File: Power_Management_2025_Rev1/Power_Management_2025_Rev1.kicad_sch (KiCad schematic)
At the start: 103 parts, among them J1 RJ45_LED_Shielded, Q1 BSS138, Q2 IPB180N10S4-02, Q3 IPB180N10S4-02, U1 Teensy4.1_DEV-16771, U10 LT1910, U11 LT1910, U12 PKE3316ZPI, U13 PKE3316ZPI, U2 OKI-78SR-3.3_1.5-W36-C, U3 ACS756xCB-050B-PFF, U4 ${SIM.PARAMS}, U5 ${SIM.PARAMS}, U6 ${SIM.PARAMS}, U7 ${SIM.PARAMS}, U8 ${SIM.PARAMS}, U9 ${SIM.PARAMS}

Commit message: Added set of andersons
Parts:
- added unit 4 of Conn21
- added Conn24: AndersonPP, symbol MRDT_Connectors:AndersonPP
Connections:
- net GND: now also Conn24.1 (GND)
- net PV: now also Conn21.4 (PV+)
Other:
- moved on the sheet: Conn19A, Conn19D, Conn1E, Conn20A, Conn20D, Conn21A, Conn22A, Conn4E

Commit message: Cleaned up schematic
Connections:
- net GND: now also U1.USB_GND1 (USB_GND), U1.USB_GND2 (USB_GND)
- no-connect marks 5 -> 47
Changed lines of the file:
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@@
 	)
 	(junction
+		(at 86.36 123.19)
+		(diameter 0)
+		(color 0 0 0 0)
+	)
+	(junction
 		(at 227.965 118.11)
 		(diameter 0)
@@
 	)
 	(no_connect
+		(at 38.1 82.55)
+	)
+	(no_connect
+		(at 196.85 248.92)
+	)
+	(no_connect
+		(at 78.74 80.01)
+	)
+	(no_connect
+		(at 78.74 77.47)
+	)
+	(no_connect
+		(at 78.74 54.61)
+	)
+	(no_connect
+		(at 275.59 238.76)
+	)
+	(no_connect
+		(at 38.1 87.63)
+	)
+	(no_connect
+		(at 38.1 39.37)
+	)
+	(no_connect
+		(at 38.1 67.31)
+	)
+	(no_connect
+		(at 38.1 62.23)
+	)
+	(no_connect
+		(at 78.74 74.93)
+	)
+	(no_connect
+		(at 78.74 113.03)
+	)
+	(no_connect
+		(at 38.1 90.17)
+	)
+	(no_connect
+		(at 78.74 100.33)
+	)
+	(no_connect
 		(at 62.23 139.7)
 	)
 	(no_connect
+		(at 38.1 85.09)
+	)
+	(no_connect
+		(at 78.74 67.31)
+	)
+	(no_connect
+		(at 38.1 59.69)
+	)
+	(no_connect
+		(at 38.1 69.85)
+	)
+	(no_connect
+		(at 38.1 46.99)
+	)
+	(no_connect
+		(at 78.74 34.29)
+	)
+	(no_connect
 		(at 62.23 142.24)
 	)
 	(no_connect
+		(at 78.74 115.57)
+	)
+	(no_connect
+		(at 78.74 102.87)
+	)
+	(no_connect
 		(at 41.91 154.94)
 	)
 	(no_connect
+		(at 78.74 97.79)
+	)
+	(no_connect
+		(at 38.1 64.77)
+	)
+	(no_connect
 		(at 365.76 166.37)
 	)
 	(no_connect
+		(at 38.1 49.53)
+	)
+	(no_connect
+		(at 41.91 149.86)
+	)
+	(no_connect
+		(at 78.74 64.77)
+	)
+	(no_connect
+		(at 78.74 110.49)
+	)
+	(no_connect
+		(at 38.1 74.93)
+	)
+	(no_connect
+		(at 78.74 26.67)
+	)
+	(no_connect
+		(at 78.74 87.63)
+	)
+	(no_connect
+		(at 38.1 113.03)
+	)
+	(no_connect
+		(at 78.74 85.09)
+	)
+	(no_connect
+		(at 38.1 41.91)
+	)
+	(no_connect
+		(at 78.74 107.95)
+	)
+	(no_connect
+		(at 78.74 31.75)
+	)
+	(no_connect
+		(at 78.74 105.41)
+	)
+	(no_connect
+		(at 78.74 95.25)
+	)
+	(no_connect
+		(at 78.74 57.15)
+	)
+	(no_connect
+		(at 38.1 72.39)
+	)
+	(no_connect
 		(at 364.49 226.06)
 	)
+	(no_connect
+		(at 78.74 62.23)
+	)
+	(no_connect
+		(at 38.1 77.47)
+	)
 	(wire
 		(pts
@@
 	(wire
 		(pts
-			(xy 86.36 120.65) (xy 86.36 127)
+			(xy 86.36 120.65) (xy 86.36 123.19)
 		)
 		(stroke
@@
 	(wire
 		(pts
+			(xy 86.36 123.19) (xy 86.36 127)
+		)
+		(stroke
+			(width 0)
+			(type default)
+		)
+	)
+	(wire
+		(pts
 			(xy 118.11 229.87) (xy 124.46 229.87)
 		)
@@
 		)
 		(stroke
+			(width 0)
+			(type default)
+		)
+	)
+	(wire
+		(pts
+			(xy 78.74 123.19) (xy 86.36 123.19)
+		)
+		(stroke

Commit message: Made Changes from word doc
flipped power flags on current sensing, switched all PV pins to +BATT, added labels to LEDs, removed pull down resistor from buzzer circuit and flipped polarity of buzzer, Changed LED resistors to 1.5k and the 3.3V resistor to 100, Changed vias to mounting holes, Tied ethernet pin 5 to pin 2 before the capacitor, added no connection to the timers on the gate drivers, changed the 10uF caps on the gate drivers to polarized caps, changed all labels so that they are consistent with each other, switched order of cell connectors,
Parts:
- removed C8, C9: 10uF, symbol Device:C
- removed R2: 4.7k, symbol Device:R
- removed V1, V2, V3, V4: Via, symbol MRDT_Drill_Holes:Via
- added C14, C9: 10uF, symbol Device:C_Polarized_Small_US
- added H1, H2, H3, H4: MountingHole, symbol Mechanical:MountingHole
- C1, C2: value 10u -> 10uF
- C10, C12: value 22uf -> 22uF
- C11, C13: value 10uf -> 10uF
- C5: value 1000uf -> 1000uF
- D10, D4, D5, D6, D7, D8, D9: value LED -> GREEN
- R29: value 2k -> 100
- R30, R31, R32, R33, R34, R35: value 2k -> 1.5k
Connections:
- net +24V is gone; now on net +BATT: C1.1, U2.1 (IN)
- net Buzzer is gone; now on net GND: Q1.1 (G), U1.22 (A8)
- net LowCurrent_PWR is gone; now on net Low_Current_PWR: Conn14.4 (PV+), Conn15.4 (PV+), Conn16.4 (PV+), Conn17.4 (PV+), Conn18.4 (PV+), R34.1
- net M_Power is gone; now on net Motor_PWR: Q3.2 (S), Q3.3 (S), Q3.5 (S), Q3.6 (S), Q3.7 (S)
- net NS 24V is gone; now on net NS_24V: C12.2, C13.2, U13.4 (VOUT+)
- net POE 24V is gone; now on net POE_24V: C10.2, C11.2, U12.4 (VOUT+)
- net +3.3V: now also B1.1 (V+); no longer B1.2 (V-)
- net +BATT: now also C4.1, C5.1, C6.1, C7.1, Conn1.1, Conn19.4 (PV+), Conn20.4 (PV+), Conn21.4 (PV+), Conn4.1, D1.1 (K), D2.1 (K), Q2.4 (D), Q3.4 (D), U10.8 (V+), U11.8 (V+), U12.3 (VIN+), U13.3 (VIN+), U3.4 (IP+), U4.3 (V+), U5.3 (V+), U6.3 (V+), U7.3 (V+), U8.3 (V+), U9.3 (V+), C14.1, C9.1; no longer U3.5 (IP-)
- net CELL_SENSE_1: now also Conn2.6; no longer Conn2.1
- net CELL_SENSE_2: now also Conn2.5; no longer Conn2.2
- net CELL_SENSE_3: now also Conn2.4; no longer Conn2.3
- net CELL_SENSE_4: now also Conn2.3; no longer Conn2.4
- net CELL_SENSE_5: now also Conn2.2; no longer Conn2.5
- net CELL_SENSE_6: now also Conn2.1; no longer Conn2.6
- net GND: now also C14.2, C9.2; no longer U10.2 (TIMER), U11.2 (TIMER)
- net LC_en: now also U1.9 (OUT1C)
- net PV: now also U3.5 (IP-); no longer C4.1, C5.1, C6.1, C7.1, Conn1.1, Conn19.4 (PV+), Conn20.4 (PV+), Conn21.4 (PV+), Conn4.1, D1.1 (K), D2.1 (K), Q2.4 (D), Q3.4 (D), U10.8 (V+), U11.8 (V+), U12.3 (VIN+), U13.3 (VIN+), U3.4 (IP+), U4.3 (V+), U5.3 (V+), U6.3 (V+), U7.3 (V+), U8.3 (V+), U9.3 (V+)
- net at D3.1 (K), Q1.3 (D): now also B1.2 (V-); no longer B1.1 (V+)
- net at C3.1, J1.2: now also J1.5
- net Cell_Sense1 renamed Cell_Sense_1
- net Cell_Sense2 renamed Cell_Sense_2
- net Cell_Sense3 renamed Cell_Sense_3
- net Cell_Sense4 renamed Cell_Sense_4
- net Cell_Sense5 renamed Cell_Sense_5
- net Cell_Sense6 renamed Cell_Sense_6
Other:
- note added: "Mounting Holes"
- note removed: "VIA's for mounting"
- moved on the sheet: B1, C3, D10, D7, D8, D9

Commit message: Finished changes
removed additional andersons, capitalized all labels, added another gat driver circuit (unfinished)
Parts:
- removed C12: 22uF, symbol Device:C
- removed unit 5 of Conn1
- removed Conn19, Conn20, Conn21, Conn22, Conn24: AndersonPP, symbol MRDT_Connectors:AndersonPP
- removed unit 5 of Conn4
- removed Conn9: AndersonPP, MRDT_Connectors:Square_Anderson_2_H_Stacked, symbol MRDT_Connectors:AndersonPP
- added C12: 10uF, symbol Device:C_Polarized_Small_US
- added C8: 22uF, symbol Device:C
- added Q4: IPB180N10S4-02, Package_TO_SOT_SMD:TO-263-6, symbol Transistor_FET:IPB180N10S4-02
- added R2: 5.1k, symbol Device:R
- added U14: LT1910, symbol MRDT_ICs:LT1910
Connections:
- net Cell_Sense_1 is gone; now on net CELL_SENSE_1: R4.1, U1.15 (A1), U7.5
- net Cell_Sense_2 is gone; now on net CELL_SENSE_2: R10.1, U1.16 (A2), U4.5
- net Cell_Sense_3 is gone; now on net CELL_SENSE_3: R14.1, U1.17 (A3), U5.5
- net Cell_Sense_4 is gone; now on net CELL_SENSE_4: R18.1, U1.18 (A4), U6.5
- net Cell_Sense_5 is gone; now on net CELL_SENSE_5: R22.1, U1.19 (A5), U8.5
- net Cell_Sense_6 is gone; now on net CELL_SENSE_6: R26.1, U1.20 (A6), U9.5
- net Temp_sense is gone; now on net TEMP_SENSE: Conn23.2
- net +5V: now also R2.1
- net +BATT: now also R35.1, U10.6 (SENSE), U11.6 (SENSE), C12.1, Q4.4 (D), U14.6 (SENSE), U14.8 (V+)
- net GND: now also C12.2, C8.1, U14.1 (GND); no longer Q1.1 (G), U1.22 (A8)
- net NS_24V: now also C8.2
- net TEMP_SENSE: now reaches U1.21 (A7)
- net ESTOP: now reaches U1.41 (A17)
- net Aux_PWR renamed AUX_PWR
- net C_Sense renamed C_SENSE
- net Cell1 renamed CELL1
- net Cell2 renamed CELL2
- net Cell3 renamed CELL3
- net Cell4 renamed CELL4
- net Cell5 renamed CELL5
- net Cell6 renamed CELL6
- net Current_Sense renamed CURRENT_SENSE
- net LC_en renamed LC_EN
- net Low_Current_PWR renamed LOW_CURRENT_PWR
- net Motor_PWR renamed MOTOR_PWR
- net Motor_en renamed MOTOR_EN
- net NS_Enable renamed NS_ENABLE
- net POE_Enable renamed POE_ENABLE
- net PV renamed PACK_OUT
- net PACK_OUT: no longer R35.1
- new net: R2.2, U14.3 (FAULT)
- new net: Q4.1 (G), U14.5 (GATE)
- new net: Q4.2 (S), Q4.3 (S), Q4.5 (S), Q4.6 (S), Q4.7 (S)
- new net BUZZER: Q1.1 (G), U1.22 (A8)
- no-connect marks 47 -> 44

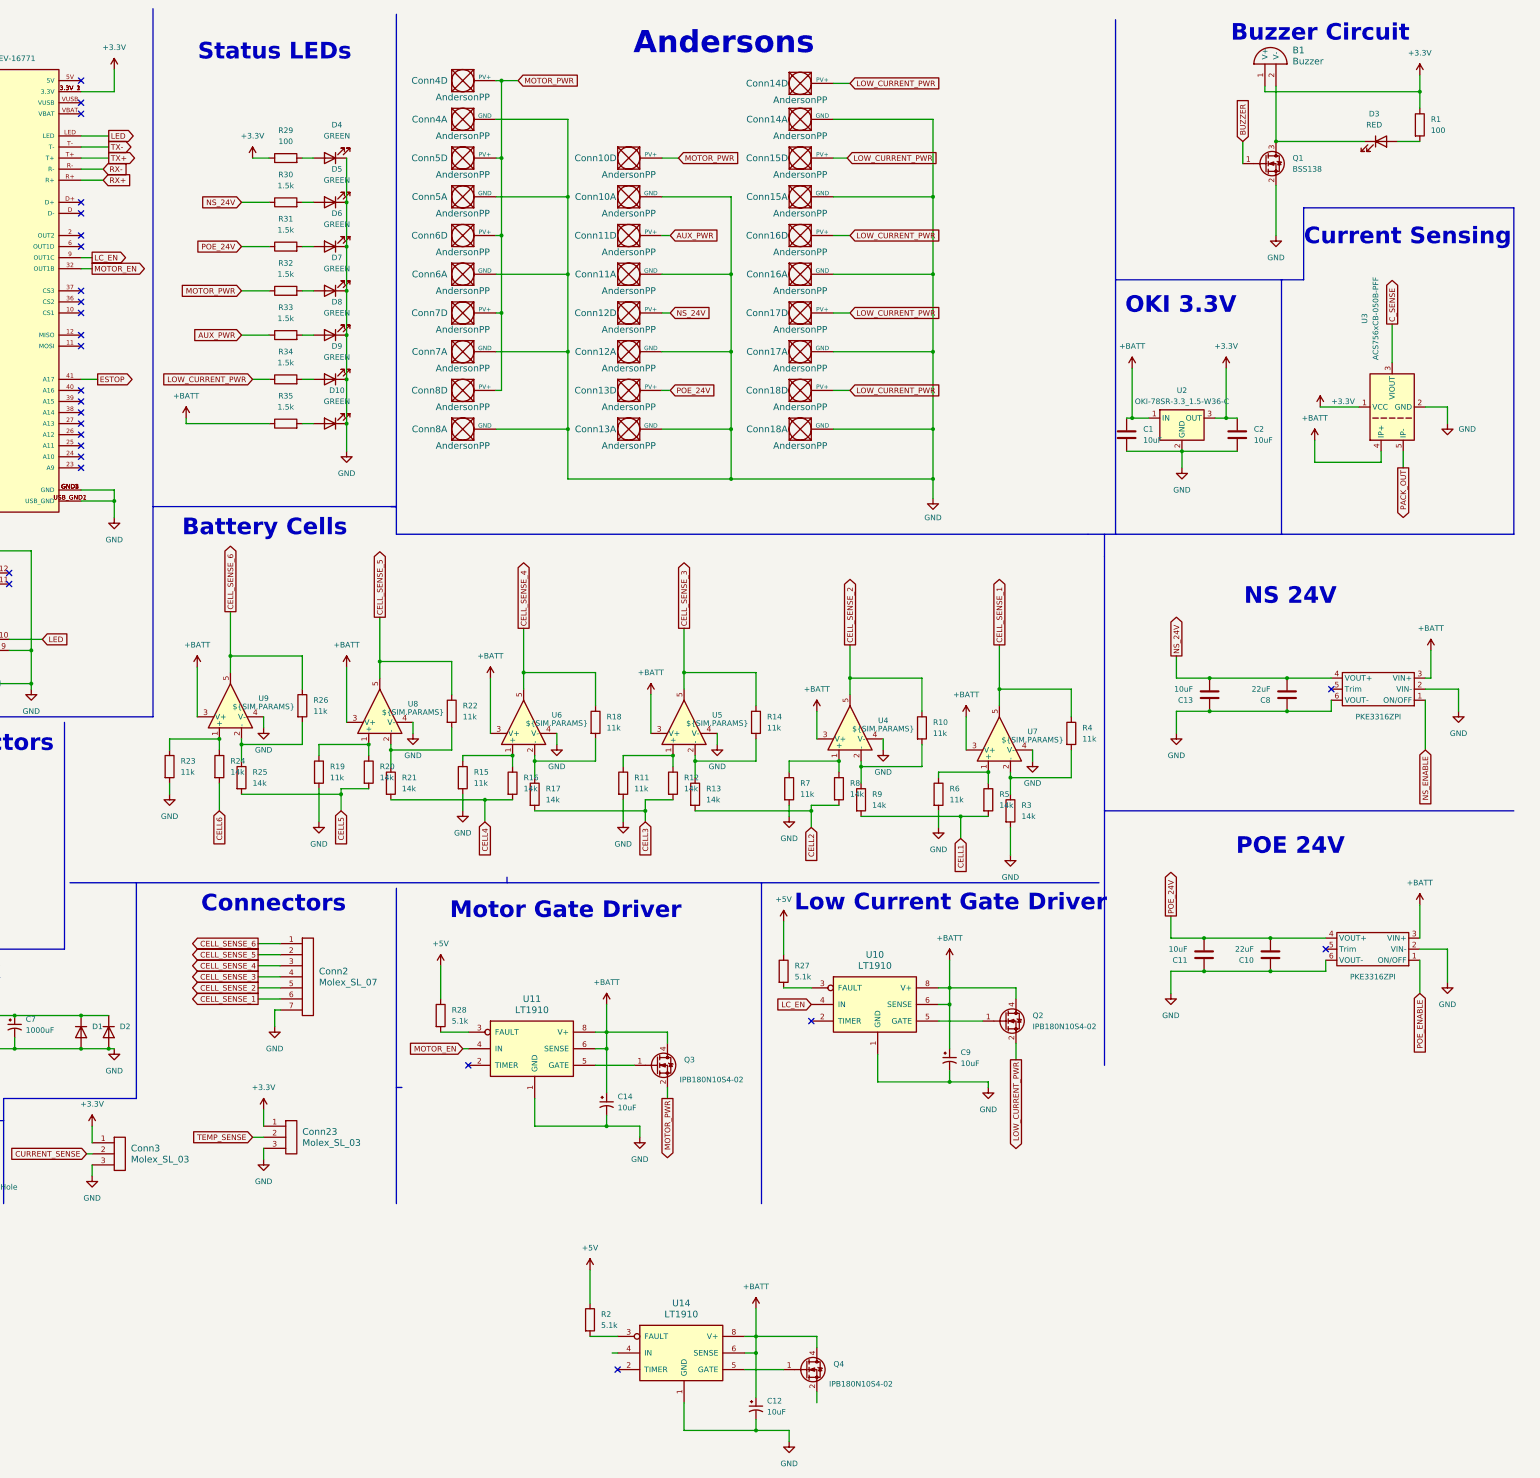
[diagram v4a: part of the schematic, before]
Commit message: Added aux gate driver
rearranged some of the circuits to make room for AUX gate driver
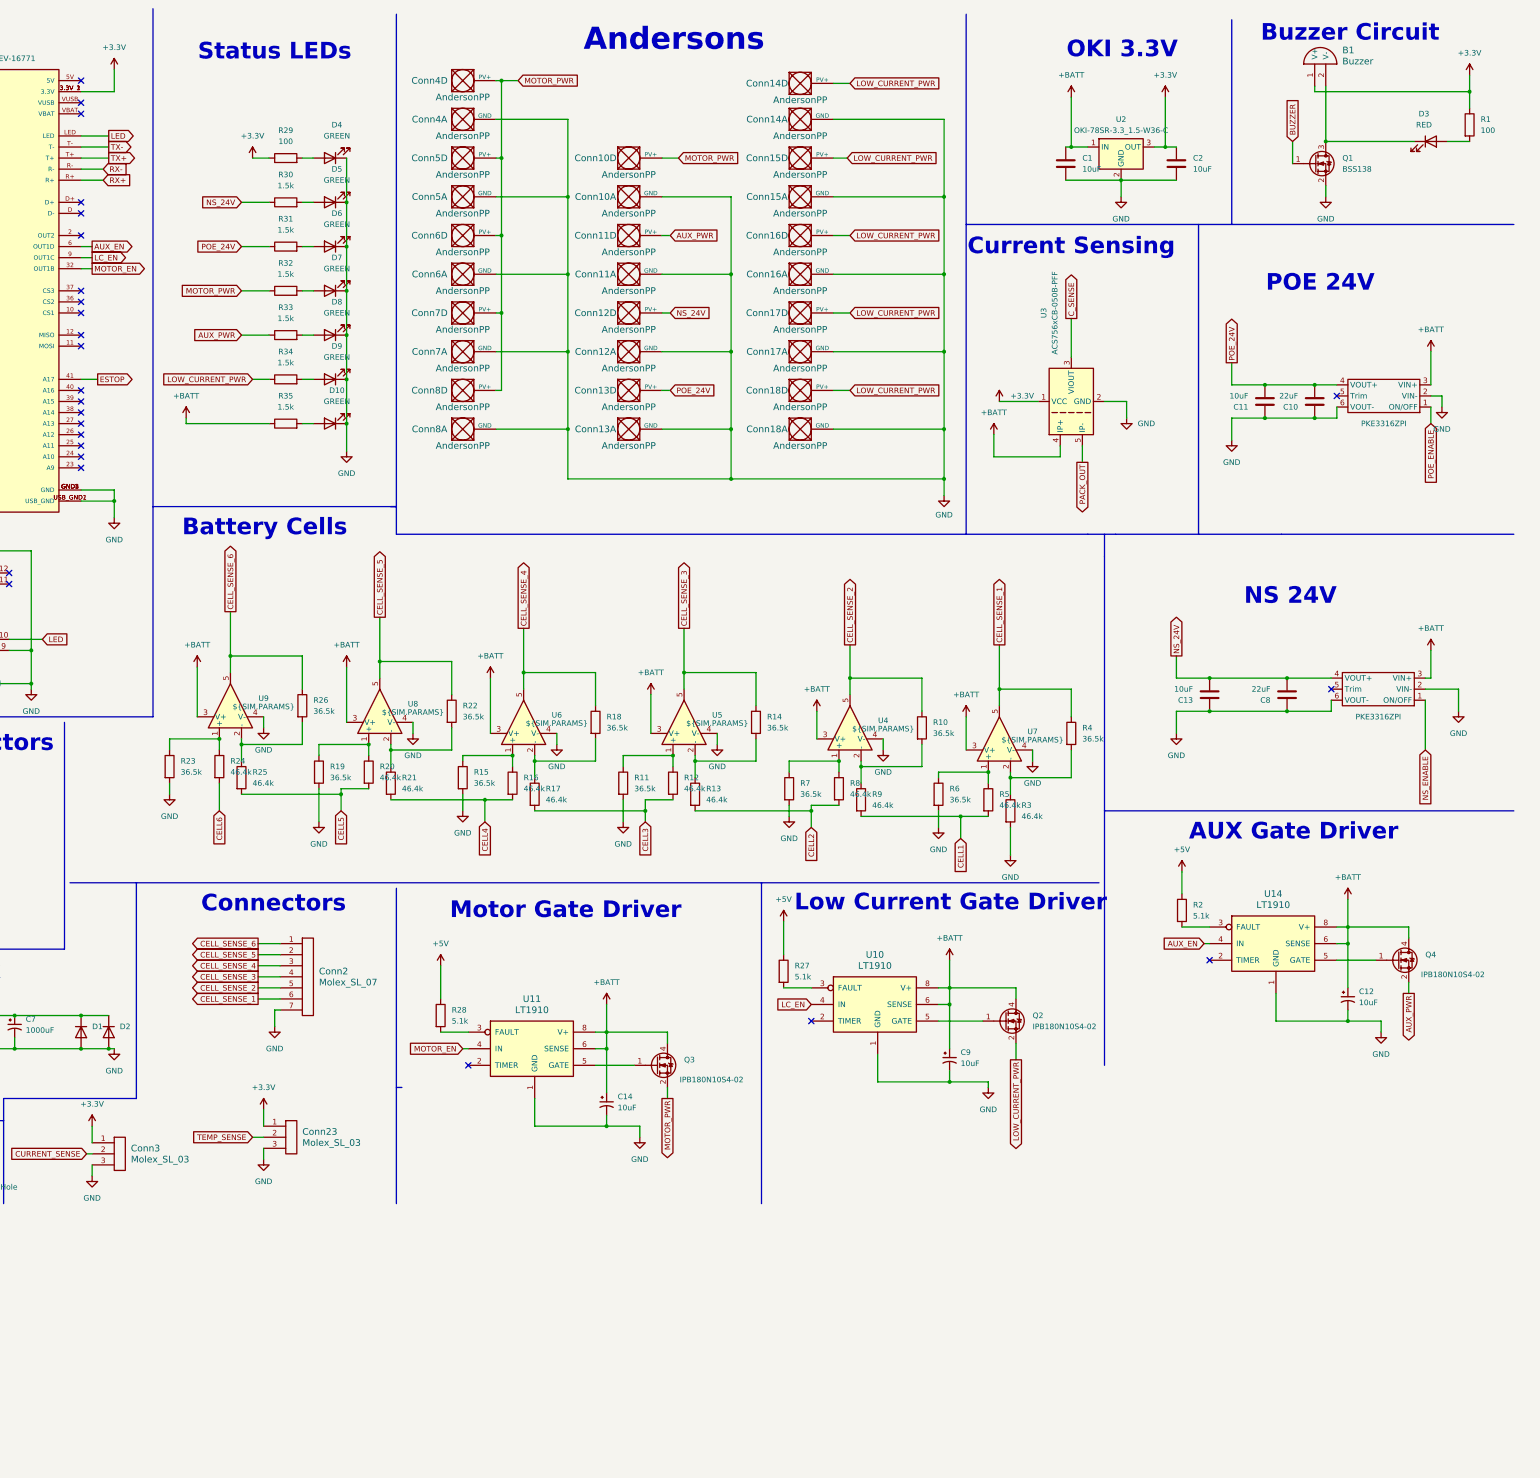
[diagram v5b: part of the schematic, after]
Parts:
- R10, R11, R14, R15, R18, R19, R22, R23, R26, R4, R6, R7: value 11k -> 36.5k
- R12, R13, R16, R17, R20, R21, R24, R25, R3, R5, R8, R9: value 14k -> 46.4k
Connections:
- net AUX_PWR: now also Q4.2 (S), Q4.3 (S), Q4.5 (S), Q4.6 (S), Q4.7 (S)
- net AUX_EN: now reaches U1.6 (OUT1D)
- net AUX_EN: now also U14.4 (IN)
- no-connect marks 44 -> 43
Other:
- note added: "AUX Gate Driver"
- moved on the sheet: B1, C1, C10, C11, C12, C2, D3, Q1, Q4, R1, R2, U14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
